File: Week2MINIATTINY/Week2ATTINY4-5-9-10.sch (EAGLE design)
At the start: 27 parts

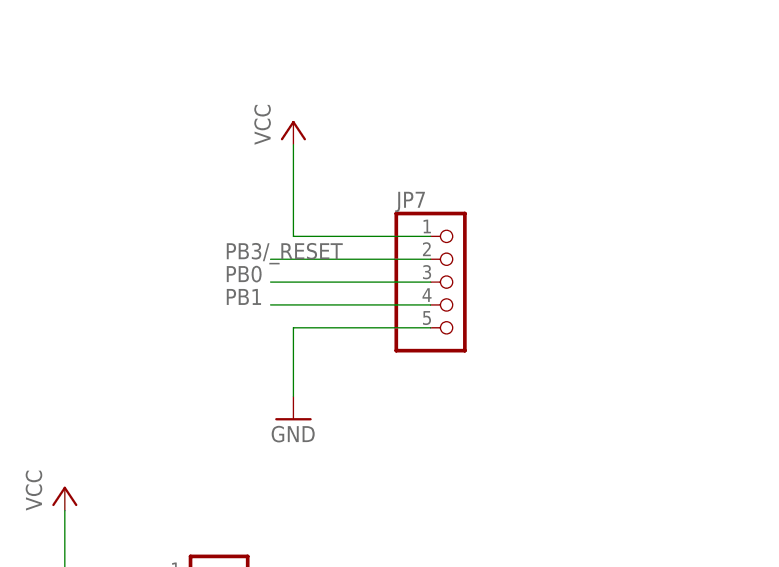
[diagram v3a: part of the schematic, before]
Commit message: week 2 routing cleaned started silk
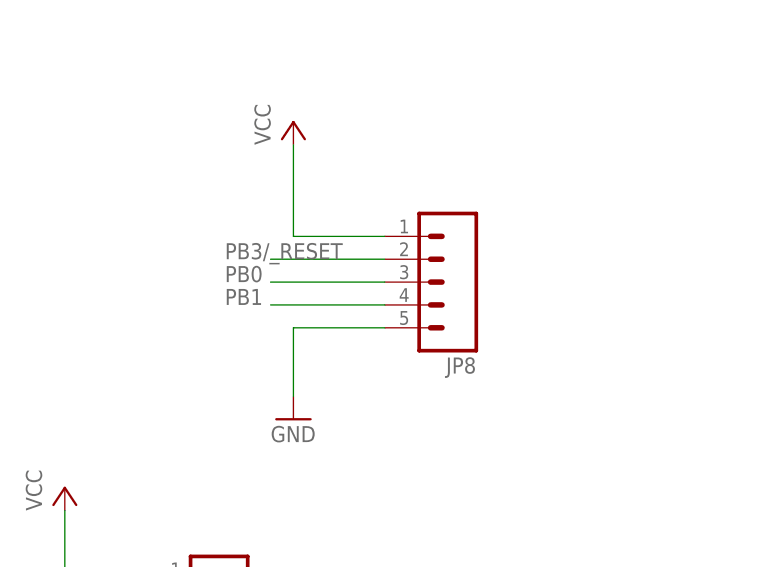
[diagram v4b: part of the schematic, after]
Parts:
- removed JP7: (no value), pinhead:PINHD-1X5
- added JP8: (no value), SparkFun-Connectors:M05NO_SILK
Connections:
- net GND: now also JP8.5; no longer JP7.5
- net PB0: now also JP8.3; no longer JP7.3
- net PB1: now also JP8.4; no longer JP7.4
- net PB3/_RESET: now also JP8.2; no longer JP7.2
- net VCC: now also JP8.1; no longer JP7.1
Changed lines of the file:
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@@
 <?xml version="1.0" encoding="utf-8"?>
 <!DOCTYPE eagle SYSTEM "eagle.dtd">
-<eagle version="7.7.0">
+<eagle version="8.4.3">
 <drawing>
 <settings>
 <setting alwaysvectorfont="yes"/>
+<setting keepoldvectorfont="yes"/>
 <setting verticaltext="up"/>
 </settings>
@@
 <part name="R10" library="rcl" deviceset="R-EU_" device="R0603"/>
 <part name="GND9" library="supply1" deviceset="GND" device=""/>
-<part name="JP7" library="pinhead" deviceset="PINHD-1X5" device=""/>
 <part name="P+9" library="supply1" deviceset="VCC" device=""/>
 <part name="GND10" library="supply1" deviceset="GND" device=""/>
+<part name="JP8" library="SparkFun-Connectors" deviceset="M05" device="NO_SILK"/>
 </parts>
 <sheets>
@@
 <instance part="R10" gate="G$1" x="170.18" y="152.4" rot="R180"/>
 <instance part="GND9" gate="1" x="193.04" y="142.24"/>
-<instance part="JP7" gate="A" x="68.58" y="109.22"/>
 <instance part="P+9" gate="VCC" x="50.8" y="127"/>
 <instance part="GND10" gate="1" x="50.8" y="93.98"/>
+<instance part="JP8" gate="G$1" x="68.58" y="109.22" rot="R180"/>
 </instances>
 <busses>
@@
 </segment>
 <segment>
-<pinref part="JP7" gate="A" pin="2"/>
-<wire x1="66.04" y1="111.76" x2="48.26" y2="111.76" width="0.1524" layer="91"/>
+<wire x1="60.96" y1="111.76" x2="48.26" y2="111.76" width="0.1524" layer="91"/>
 <label x="43.18" y="111.76" size="1.778" layer="95"/>
+<pinref part="JP8" gate="G$1" pin="2"/>
 </segment>
 </net>
@@
 </segment>
 <segment>
-<pinref part="JP7" gate="A" pin="3"/>
-<wire x1="66.04" y1="109.22" x2="48.26" y2="109.22" width="0.1524" layer="91"/>
+<wire x1="60.96" y1="109.22" x2="48.26" y2="109.22" width="0.1524" layer="91"/>
 <label x="43.18" y="109.22" size="1.778" layer="95"/>
+<pinref part="JP8" gate="G$1" pin="3"/>
 </segment>
 </net>
@@
 </segment>
 <segment>
-<pinref part="JP7" gate="A" pin="4"/>
-<wire x1="66.04" y1="106.68" x2="48.26" y2="106.68" width="0.1524" layer="91"/>
+<wire x1="60.96" y1="106.68" x2="48.26" y2="106.68" width="0.1524" layer="91"/>
 <label x="43.18" y="106.68" size="1.778" layer="95"/>
+<pinref part="JP8" gate="G$1" pin="4"/>
 </segment>
 </net>
@@
 </segment>
 <segment>
-<pinref part="JP7" gate="A" pin="5"/>
-<wire x1="66.04" y1="104.14" x2="50.8" y2="104.14" width="0.1524" layer="91"/>
+<wire x1="60.96" y1="104.14" x2="50.8" y2="104.14" width="0.1524" layer="91"/>
 <wire x1="50.8" y1="104.14" x2="50.8" y2="96.52" width="0.1524" layer="91"/>
 <pinref part="GND10" gate="1" pin="GND"/>
+<pinref part="JP8" gate="G$1" pin="5"/>
 </segment>
 </net>
@@
 </segment>
 <segment>
-<pinref part="JP7" gate="A" pin="1"/>
-<wire x1="66.04" y1="114.3" x2="50.8" y2="114.3" width="0.1524" layer="91"/>
+<wire x1="60.96" y1="114.3" x2="50.8" y2="114.3" width="0.1524" layer="91"/>
 <wire x1="50.8" y1="114.3" x2="50.8" y2="124.46" width="0.1524" layer="91"/>
 <pinref part="P+9" gate="VCC" pin="VCC"/>
-</segment>
-</net>
+<pinref part="JP8" gate="G$1" pin="1"/>
+</segment>
+</net>

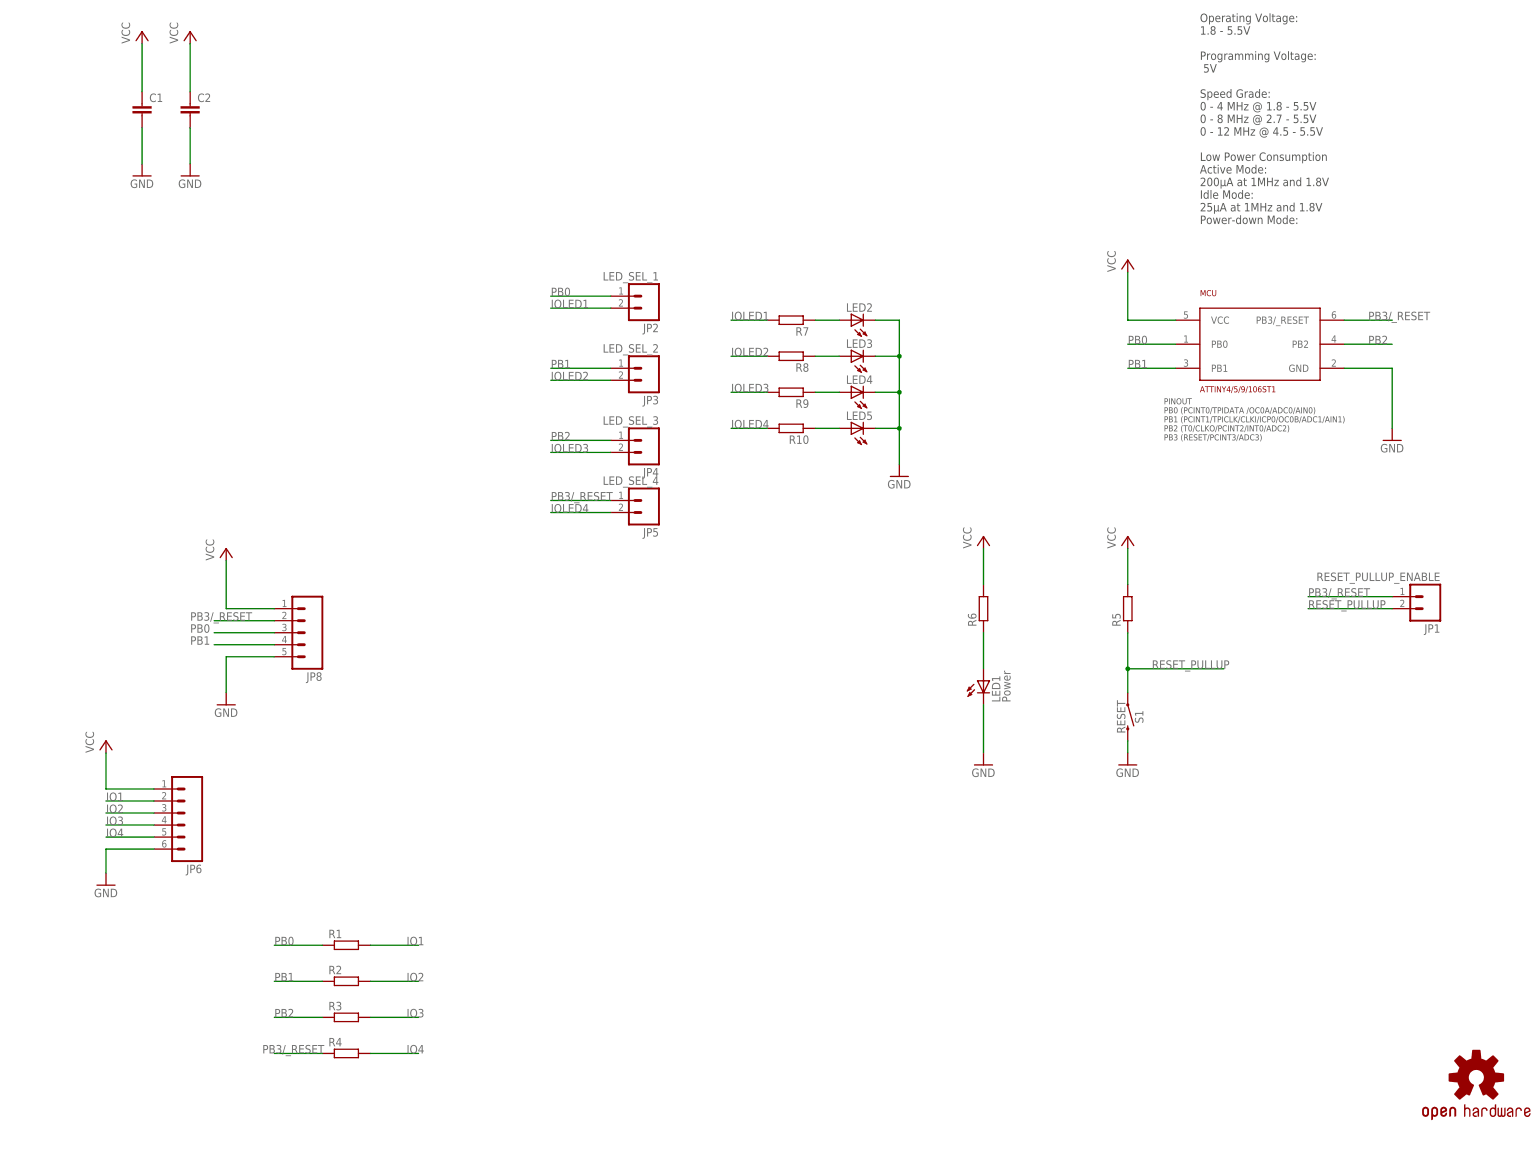
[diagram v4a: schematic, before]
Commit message: Week2 Schmatic finished
Week2 Schmatic finished and tidied up ERC check done values and labels added, added CC-BY Licence details and readme updated
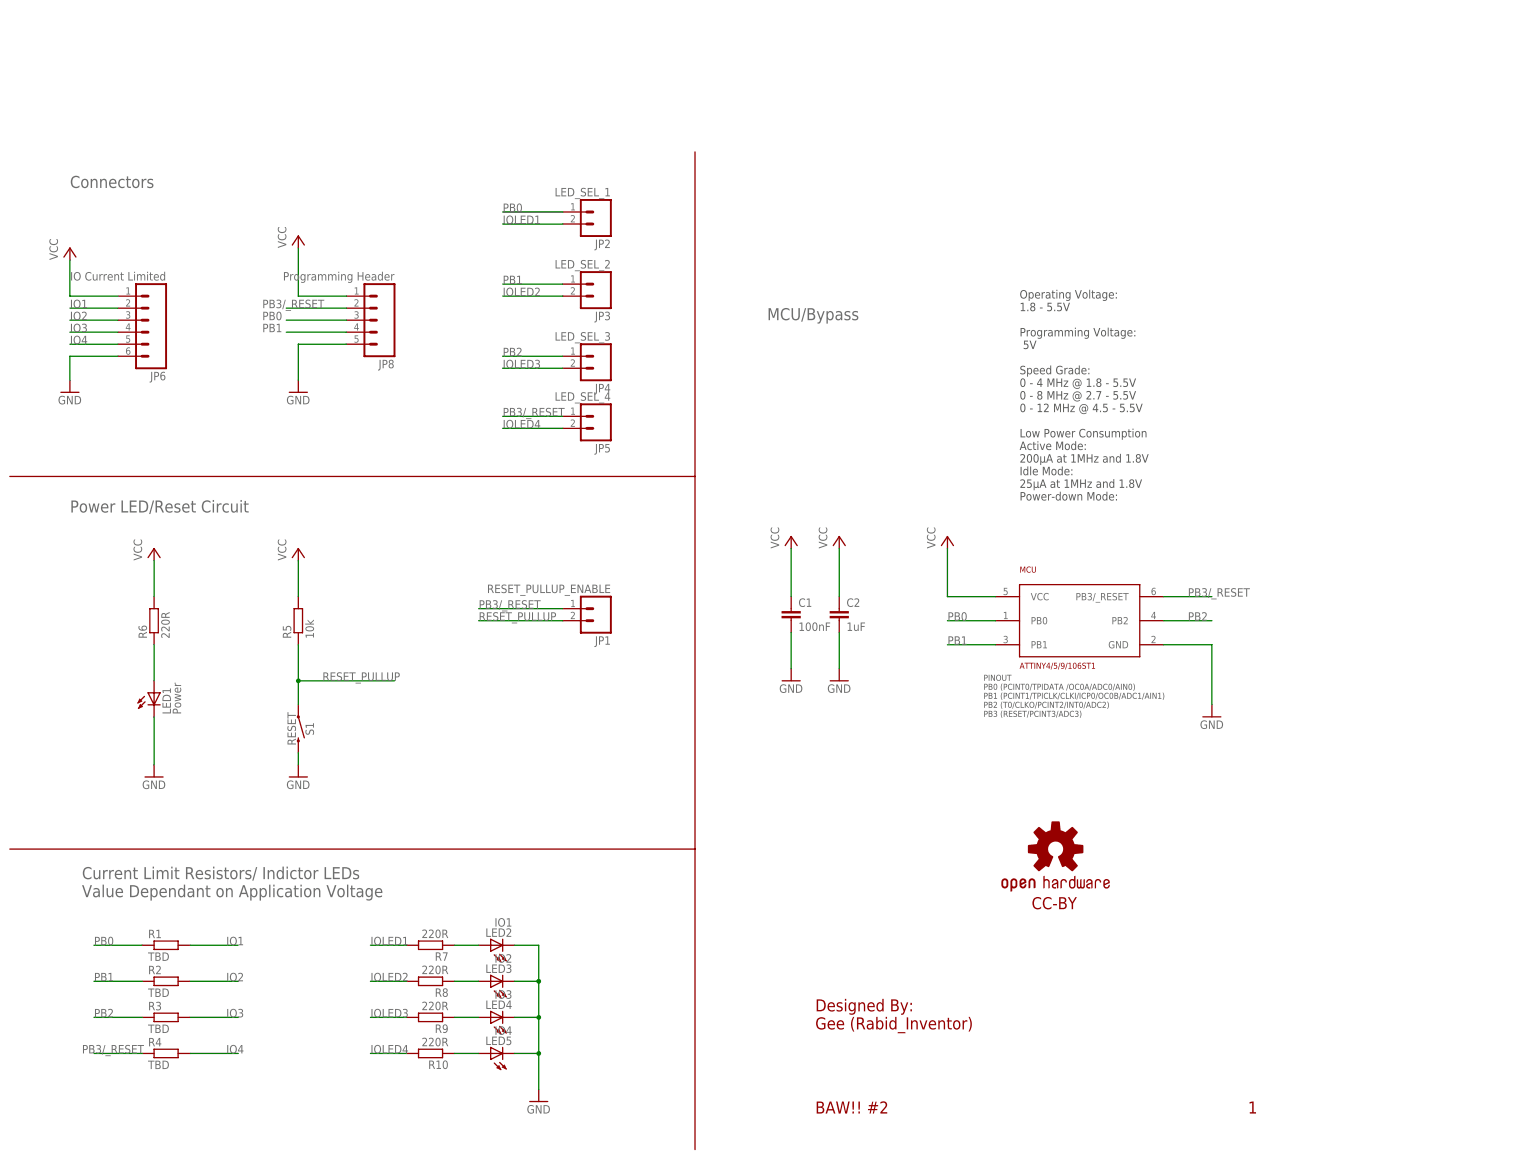
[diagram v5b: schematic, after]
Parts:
- C1: value (none) -> 100nF
- C2: value (none) -> 1uF
- JP6: value (none) -> IO Current Limited
- JP8: value (none) -> Programming Header
- LED2: value (none) -> IO1
- LED3: value (none) -> IO2
- LED4: value (none) -> IO3
- LED5: value (none) -> IO4
- R1, R2, R3, R4: value (none) -> TBD
- R10, R6, R7, R8, R9: value (none) -> 220R
- R5: value (none) -> 10k
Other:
- note added: "1"
- note added: "BAW!! #2"
- note added: "CC-BY"
- note added: "Connectors"
- note added: "Current Limit Resistors/ Indictor LEDs Value Dependant on Application Voltage"
- note added: "Designed By: Gee (Rabid_Inventor)"
- note added: "MCU/Bypass"
- note added: "Power LED/Reset Circuit"
- moved on the sheet: C1, C2, JP1, JP2, JP3, JP4, JP5, JP6, JP8, LED1, LED2, LED3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
